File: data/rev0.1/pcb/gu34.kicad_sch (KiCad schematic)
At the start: 69 parts, among them SW1 SW_PUSH, SW10 SW_PUSH, SW11 SW_PUSH, SW12 SW_PUSH, SW13 SW_PUSH, SW14 SW_PUSH, SW15 SW_PUSH, SW16 SW_PUSH, SW17 SW_PUSH, SW18 SW_PUSH, SW19 SW_PUSH, SW2 SW_PUSH, SW20 SW_PUSH, SW21 SW_PUSH, SW22 SW_PUSH, SW23 SW_PUSH, SW24 SW_PUSH, SW25 SW_PUSH, SW26 SW_PUSH, SW27 SW_PUSH, SW28 SW_PUSH, SW29 SW_PUSH, SW3 SW_PUSH, SW30 SW_PUSH, SW31 SW_PUSH, SW32 SW_PUSH, SW33 SW_PUSH, SW34 SW_PUSH, SW4 SW_PUSH, SW5 SW_PUSH, SW6 SW_PUSH, SW7 SW_PUSH, SW8 SW_PUSH, SW9 SW_PUSH

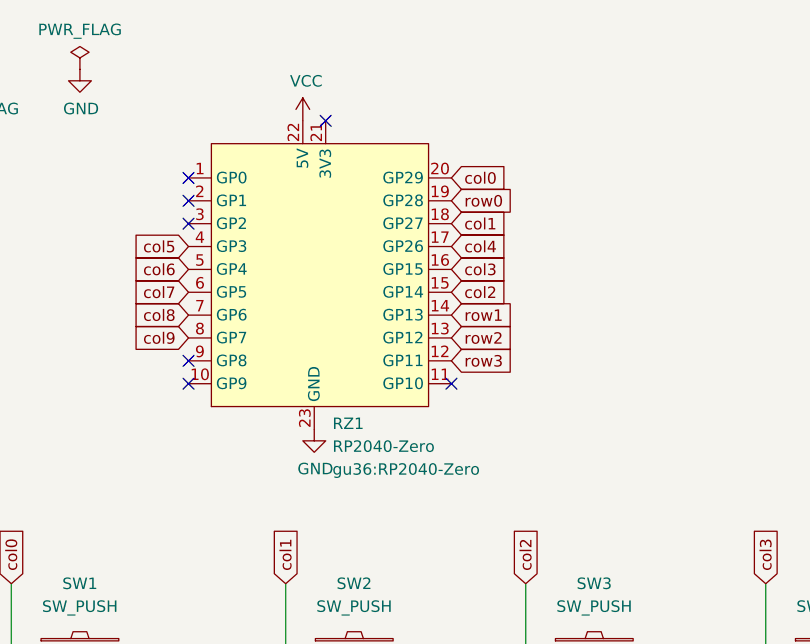
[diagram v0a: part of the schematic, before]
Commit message: rp2040 zero のフットプリントとシンボルが正しくなかったため、修正した
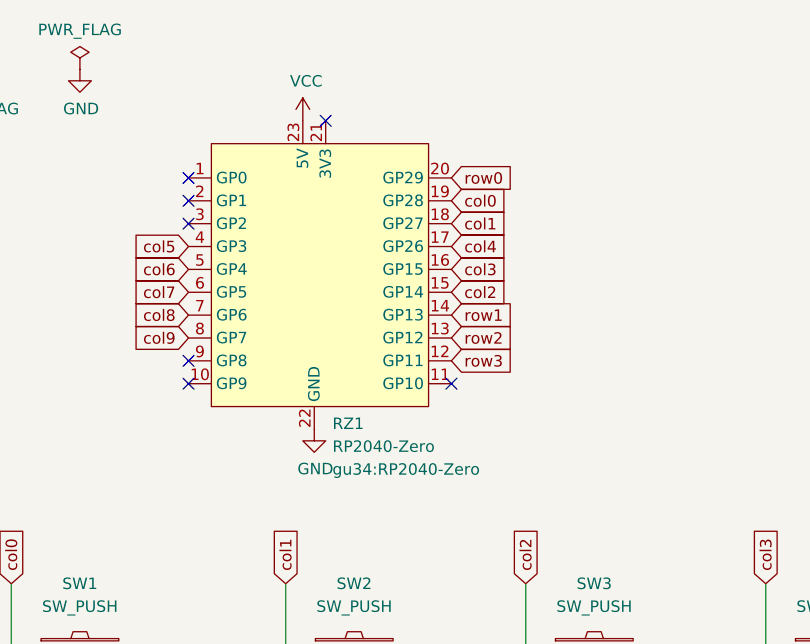
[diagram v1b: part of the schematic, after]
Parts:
- D1, D10, D11, D12, D13, D14, D15, D16, D17, D18, D19, D2, D20, D21, D22, D23, D24, D25, D26, D27, D28, D29, D3, D30, D31, D32, D33, D34, D4, D5, D6, D7, D8, D9: footprint gu36:Diode_SMD -> gu34:Diode_SMD
- RZ1: footprint gu36:RP2040-Zero -> gu34:RP2040-Zero
- SW1, SW10, SW11, SW12, SW13, SW14, SW15, SW16, SW17, SW18, SW19, SW2, SW20, SW21, SW22, SW23, SW24, SW25, SW26, SW27, SW28, SW29, SW3, SW30, SW31, SW32, SW33, SW34, SW4, SW5, SW6, SW7, SW8, SW9: footprint gu36:SW_Choc -> gu34:SW_Choc
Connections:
- net GND: now also RZ1.22 (GND); no longer RZ1.23 (GND)
- net VCC: now also RZ1.23 (5V); no longer RZ1.22 (5V)
- net col0: now also RZ1.19 (GP28); no longer RZ1.20 (GP29)
- net row0: now also RZ1.20 (GP29); no longer RZ1.19 (GP28)
